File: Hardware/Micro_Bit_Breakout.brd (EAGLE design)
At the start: 68.6 x 20.3 mm, 11 parts, among them J1 EDGE-80PTH-RA, J2 M22PTH

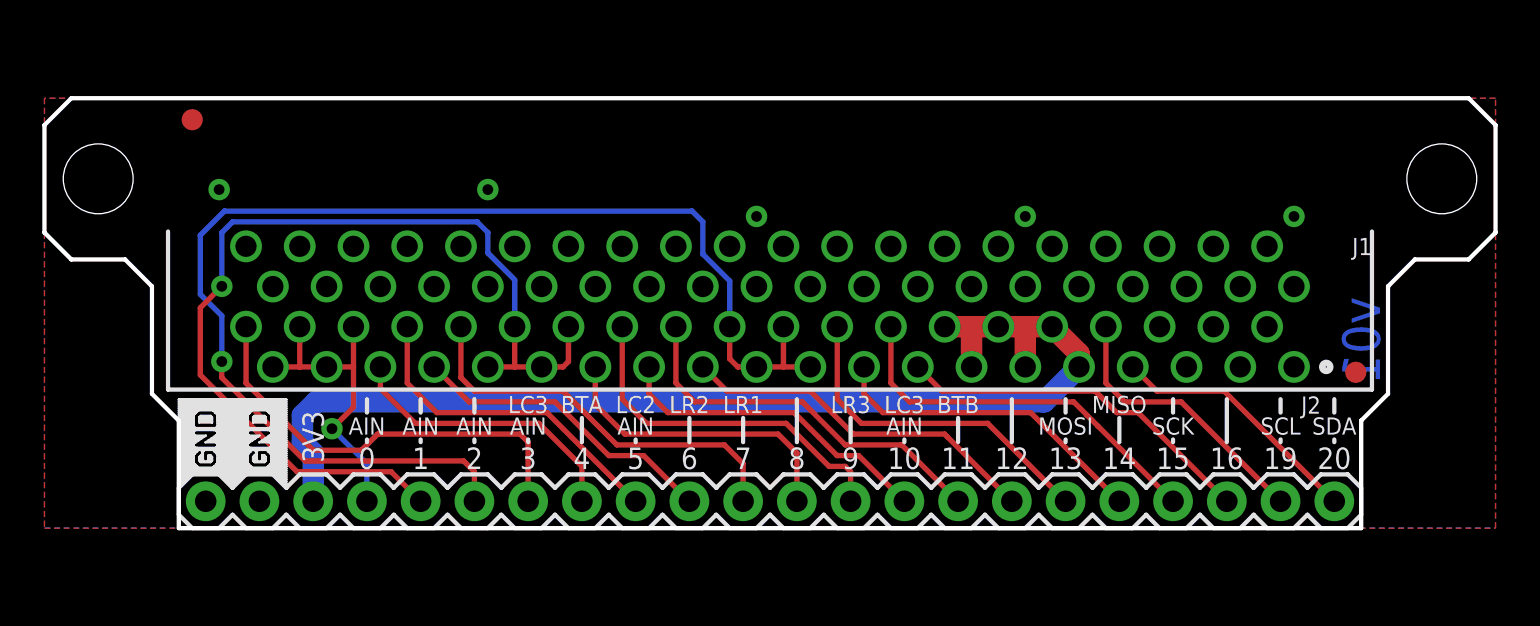
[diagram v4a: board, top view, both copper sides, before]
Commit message: Changed pins to match new micro:bit pinout. Updated to v10. Ready for review.
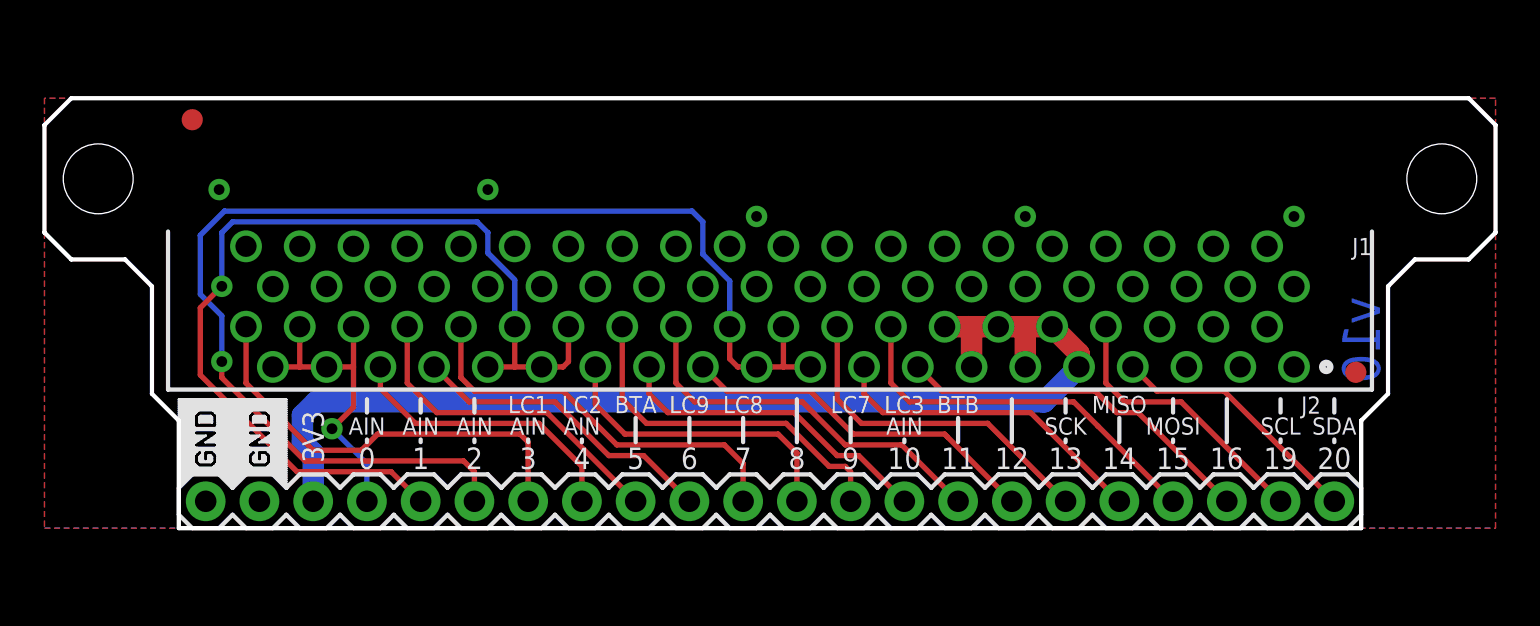
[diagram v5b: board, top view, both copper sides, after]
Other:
- board text added: "LC1"
- board text added: "LC7"
- board text added: "LC8"
- board text added: "LC9"
- board text added: "v10"
- board text removed: "LR1"
- board text removed: "LR2"
- board text removed: "LR3"
- board text removed: "v01"

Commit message: Moved top up 0.1 inches. Added bottom fiducials. Added dimensions note for measurements.
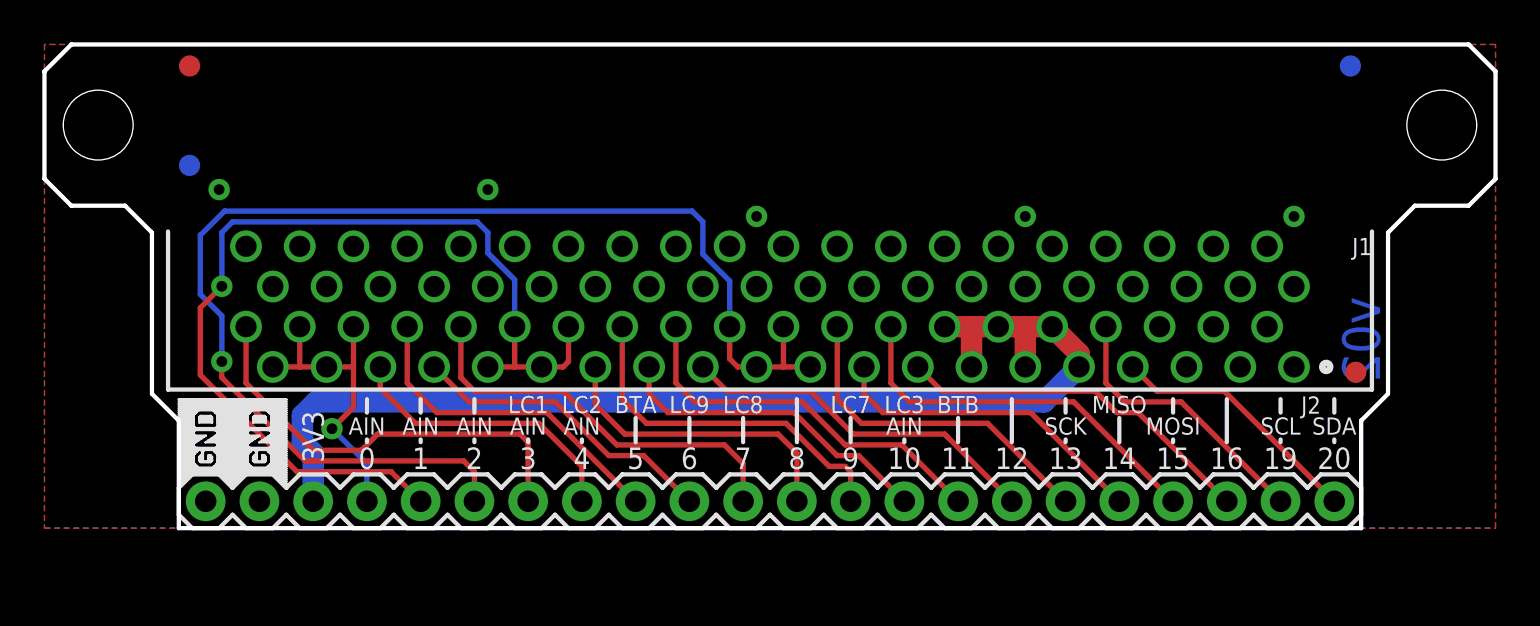
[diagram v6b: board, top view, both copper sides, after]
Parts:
- added FD3, FD4: FIDUCIAL1X2, SparkFun-Aesthetics:FIDUCIAL-1X2
- moved FD1 2.54 mm to (6.86, 21.8)
- moved H1 2.54 mm to (2.54, 19.1)
- moved H2 2.54 mm to (66.0, 19.1)
- moved LOGO3 1.92 mm to (12.7, 19.1)
- moved LOGO2 1.91 mm to (60.3, 16.5)
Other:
- board size 68.6 x 20.3 mm -> 68.6 x 22.9 mm
- board text added: "* All dimensions are in inches"
- board text added: "v02"
- board text removed: "v10"
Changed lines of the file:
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@@
 <setting verticaltext="up"/>
 </settings>
-<grid distance="0.05" unitdist="inch" unit="inch" style="dots" multiple="1" display="yes" altdistance="0.005" altunitdist="inch" altunit="inch"/>
+<grid distance="0.05" unitdist="inch" unit="inch" style="dots" multiple="1" display="yes" altdistance="0.025" altunitdist="inch" altunit="inch"/>
 <layers>
-<layer number="1" name="Top" color="4" fill="1" visible="no" active="yes"/>
+<layer number="1" name="Top" color="4" fill="1" visible="yes" active="yes"/>
 <layer number="2" name="Route2" color="1" fill="3" visible="no" active="yes"/>
 <layer number="15" name="Route15" color="4" fill="6" visible="no" active="yes"/>
@@
 <layer number="19" name="Unrouted" color="6" fill="1" visible="yes" active="yes"/>
 <layer number="20" name="Dimension" color="15" fill="1" visible="yes" active="yes"/>
-<layer number="21" name="tPlace" color="16" fill="1" visible="no" active="yes"/>
+<layer number="21" name="tPlace" color="16" fill="1" visible="yes" active="yes"/>
 <layer number="22" name="bPlace" color="14" fill="1" visible="yes" active="yes"/>
-<layer number="23" name="tOrigins" color="15" fill="1" visible="no" active="yes"/>
+<layer number="23" name="tOrigins" color="15" fill="1" visible="yes" active="yes"/>
 <layer number="24" name="bOrigins" color="15" fill="1" visible="yes" active="yes"/>
 <layer number="25" name="tNames" color="7" fill="1" visible="no" active="yes"/>
@@
 <layer number="43" name="vRestrict" color="2" fill="10" visible="no" active="yes"/>
 <layer number="44" name="Drills" color="7" fill="1" visible="no" active="yes"/>
-<layer number="45" name="Holes" color="7" fill="1" visible="no" active="yes"/>
+<layer number="45" name="Holes" color="7" fill="1" visible="yes" active="yes"/>
 <layer number="46" name="Milling" color="3" fill="1" visible="no" active="yes"/>
-<layer number="47" name="Measures" color="7" fill="1" visible="no" active="yes"/>
-<layer number="51" name="tDocu" color="6" fill="1" visible="no" active="yes"/>
+<layer number="47" name="Measures" color="7" fill="1" visible="yes" active="yes"/>
+<layer number="51" name="tDocu" color="6" fill="1" visible="yes" active="yes"/>
 <layer number="52" name="bDocu" color="7" fill="1" visible="no" active="yes"/>
 <layer number="3" name="Route3" color="4" fill="3" visible="no" active="no"/>
@@
 <plain>
 <wire x1="6.35" y1="0" x2="62.23" y2="0" width="0.2032" layer="20"/>
-<wire x1="67.31" y1="20.32" x2="1.27" y2="20.32" width="0.2032" layer="20"/>
+<wire x1="67.31" y1="22.86" x2="1.27" y2="22.86" width="0.2032" layer="20"/>
 <text x="60.96" y="2.794" size="1.016" layer="21" font="vector" ratio="15" rot="SR0" align="bottom-center">20</text>
 <text x="58.42" y="2.794" size="1.016" layer="21" font="vector" ratio="15" rot="SR0" align="bottom-center">19</text>
@@
 <text x="15.24" y="2.794" size="1.016" layer="21" font="vector" ratio="15" rot="SR0" align="bottom-center">0</text>
 <text x="22.86" y="2.794" size="1.016" layer="21" font="vector" ratio="15" rot="SR0" align="bottom-center">3</text>
-<wire x1="1.27" y1="20.32" x2="0" y2="19.05" width="0.2032" layer="20"/>
-<wire x1="0" y1="19.05" x2="0" y2="13.97" width="0.2032" layer="20"/>
-<wire x1="0" y1="13.97" x2="1.27" y2="12.7" width="0.2032" layer="20"/>
-<wire x1="1.27" y1="12.7" x2="3.81" y2="12.7" width="0.2032" layer="20"/>
-<wire x1="5.08" y1="11.43" x2="5.08" y2="6.35" width="0.2032" layer="20"/>
+<wire x1="1.27" y1="22.86" x2="0" y2="21.59" width="0.2032" layer="20"/>
+<wire x1="0" y1="21.59" x2="0" y2="16.51" width="0.2032" layer="20"/>
+<wire x1="0" y1="16.51" x2="1.27" y2="15.24" width="0.2032" layer="20"/>
+<wire x1="1.27" y1="15.24" x2="3.81" y2="15.24" width="0.2032" layer="20"/>
+<wire x1="5.08" y1="13.97" x2="5.08" y2="6.35" width="0.2032" layer="20"/>
 <wire x1="5.08" y1="6.35" x2="6.35" y2="5.08" width="0.2032" layer="20"/>
 <wire x1="6.35" y1="5.08" x2="6.35" y2="0" width="0.2032" layer="20"/>
-<wire x1="3.81" y1="12.7" x2="5.08" y2="11.43" width="0.2032" layer="20"/>
-<wire x1="63.5" y1="11.43" x2="63.5" y2="6.35" width="0.2032" layer="20"/>
+<wire x1="3.81" y1="15.24" x2="5.08" y2="13.97" width="0.2032" layer="20"/>
+<wire x1="63.5" y1="13.97" x2="63.5" y2="6.35" width="0.2032" layer="20"/>
 <wire x1="63.5" y1="6.35" x2="62.23" y2="5.08" width="0.2032" layer="20"/>
 <wire x1="62.23" y1="5.08" x2="62.23" y2="0" width="0.2032" layer="20"/>
-<wire x1="64.77" y1="12.7" x2="63.5" y2="11.43" width="0.2032" layer="20"/>
-<wire x1="64.77" y1="12.7" x2="67.31" y2="12.7" width="0.2032" layer="20"/>
-<wire x1="68.58" y1="13.97" x2="67.31" y2="12.7" width="0.2032" layer="20"/>
-<wire x1="68.58" y1="19.05" x2="68.58" y2="13.97" width="0.2032" layer="20"/>
-<wire x1="67.31" y1="20.32" x2="68.58" y2="19.05" width="0.2032" layer="20"/>
+<wire x1="64.77" y1="15.24" x2="63.5" y2="13.97" width="0.2032" layer="20"/>
+<wire x1="64.77" y1="15.24" x2="67.31" y2="15.24" width="0.2032" layer="20"/>
+<wire x1="68.58" y1="16.51" x2="67.31" y2="15.24" width="0.2032" layer="20"/>
+<wire x1="68.58" y1="21.59" x2="68.58" y2="16.51" width="0.2032" layer="20"/>
+<wire x1="67.31" y1="22.86" x2="68.58" y2="21.59" width="0.2032" layer="20"/>
 <text x="31.75" y="-11.43" size="1.778" layer="51" font="vector" ratio="15">Shawn Hymel</text>
-<text x="62.23" y="8.89" size="1.778" layer="16" font="vector" ratio="15" rot="SMR270" align="center">v10</text>
-<text x="34.29" y="17.145" size="1.143" layer="22" font="vector" ratio="18" rot="MR0" align="center">Micro Bit Breakout</text>
+<text x="62.23" y="8.89" size="1.778" layer="16" font="vector" ratio="15" rot="SMR270" align="center">v02</text>
+<text x="34.29" y="18.415" size="1.143" layer="22" font="vector" ratio="18" rot="MR0" align="center">Micro Bit Breakout</text>
 <text x="58.42" y="4.826" size="0.8128" layer="21" font="vector" ratio="15" rot="SR0" align="center">SCL</text>
 <text x="60.96" y="4.826" size="0.8128" layer="21" font="vector" ratio="15" rot="SR0" align="center">SDA</text>
@@
 <dimension x1="2.54" y1="16.51" x2="0" y2="16.51" x3="1.27" y3="29.21" textsize="1.778" textratio="15" layer="47" unit="inch"/>
 <dimension x1="0" y1="0" x2="5.842" y2="27.94" x3="-35.56" y3="13.97" textsize="1.778" textratio="15" layer="47" dtype="vertical" unit="inch"/>
+<text x="-30.48" y="35.56" size="1.778" layer="47" font="vector" ratio="15">* All dimensions
+  are in inches</text>
 </plain>
 <attributes>
@@
 <attribute name="PROD_ID" value="CONN-13452" x="34.29" y="7.62" size="1.778" layer="27" rot="R180" display="off"/>
 </element>
-<element name="FD1" library="SparkFun-Aesthetics" package="FIDUCIAL-1X2" value="FIDUCIAL1X2" x="6.985" y="19.304"/>
+<element name="FD1" library="SparkFun-Aesthetics" package="FIDUCIAL-1X2" value="FIDUCIAL1X2" x="6.858" y="21.844"/>
 <element name="FD2" library="SparkFun-Aesthetics" package="FIDUCIAL-1X2" value="FIDUCIAL1X2" x="61.976" y="7.366" smashed="yes"/>
-<element name="H1" library="SparkFun-Electromechanical" package="STAND-OFF" value="STAND-OFF" x="2.54" y="16.51"/>
-<element name="H2" library="SparkFun-Electromechanical" package="STAND-OFF" value="STAND-OFF" x="66.04" y="16.51"/>
-<element name="LOGO3" library="SparkFun-Aesthetics" package="OSHW-LOGO-S" value="OSHW-LOGOS" x="12.446" y="17.145" rot="MR0"/>
-<element name="LOGO2" library="SparkFun-Aesthetics" package="SFE_LOGO_NAME_FLAME_.1" value="SFE_LOGO_NAME_FLAME.1_INCH" x="60.325" y="14.605" rot="MR0"/>
+<element name="H1" library="SparkFun-Electromechanical" package="STAND-OFF" value="STAND-OFF" x="2.54" y="19.05"/>
+<element name="H2" library="SparkFun-Electromechanical" package="STAND-OFF" value="STAND-OFF" x="66.04" y="19.05"/>
+<element name="LOGO3" library="SparkFun-Aesthetics" package="OSHW-LOGO-S" value="OSHW-LOGOS" x="12.7" y="19.05" rot="MR0"/>
+<element name="LOGO2" library="SparkFun-Aesthetics" package="SFE_LOGO_NAME_FLAME_.1" value="SFE_LOGO_NAME_FLAME.1_INCH" x="60.325" y="16.51" rot="MR0"/>
 <element name="U$1" library="negasilk" package="NEGASILK_MICRO_BIT_BREAKOUT" value="" x="6.35" y="1.905"/>
 <element name="U$2" library="negasilk" package="NEGASILK_MICRO_BIT_BREAKOUT" value="" x="11.43" y="1.905" rot="MR0"/>
+<element name="FD3" library="SparkFun-Aesthetics" package="FIDUCIAL-1X2" value="FIDUCIAL1X2" x="61.722" y="21.844" rot="MR0"/>
+<element name="FD4" library="SparkFun-Aesthetics" package="FIDUCIAL-1X2" value="FIDUCIAL1X2" x="6.858" y="17.145" rot="MR0"/>
 </elements>
 <signals>
@@
 <contactref element="J2" pad="1"/>
 <polygon width="0.254" layer="1" isolate="0.3048">
-<vertex x="0" y="20.32"/>
+<vertex x="0" y="22.86"/>
 <vertex x="0" y="0"/>
 <vertex x="68.58" y="0"/>
-<vertex x="68.58" y="20.32"/>
+<vertex x="68.58" y="22.86"/>
 </polygon>
 <polygon width="0.254" layer="16" isolate="0.3048">
-<vertex x="0" y="20.32"/>
+<vertex x="0" y="22.86"/>
 <vertex x="0" y="0"/>
 <vertex x="68.58" y="0"/>
-<vertex x="68.58" y="20.32"/>
+<vertex x="68.58" y="22.86"/>
 </polygon>
 <via x="8.255" y="16.002" extent="1-16" drill="0.508"/>
@@
 </board>
 </drawing>
+<compatibility>
+<note version="6.3" minversion="6.2.2" severity="warning">
+Since Version 6.2.2 text objects can contain more than one line,
+which will not be processed correctly with this version.
+</note>
+</compatibility>
 </eagle>
